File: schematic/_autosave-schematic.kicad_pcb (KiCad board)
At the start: 4 copper layers, 77.8 x 81.6 mm, 154 parts, among them IC1 RS0108YQ20, IC2 AS312, IC3 TPS630250RNCR, IC4 SIM7600G-H_R2, J1 SIM7155-6-1-14-A, J3 USB_C_Receptacle_USB2.0, J9 BATT_CONNECTOR, Q1 BC817, Q10 MMBT3904, Q11 MMBT3904, Q15 SI2302, Q16 SI2302, Q8 NCE6005AR, Q9 NCE6005AR, U10 TPS56339DDC, U2 MT3608, U3 AM2302, U4 TP4056, U6 ESP32-WROOM-32, U8 CH340T(SSOP20W), Y1 12MHz

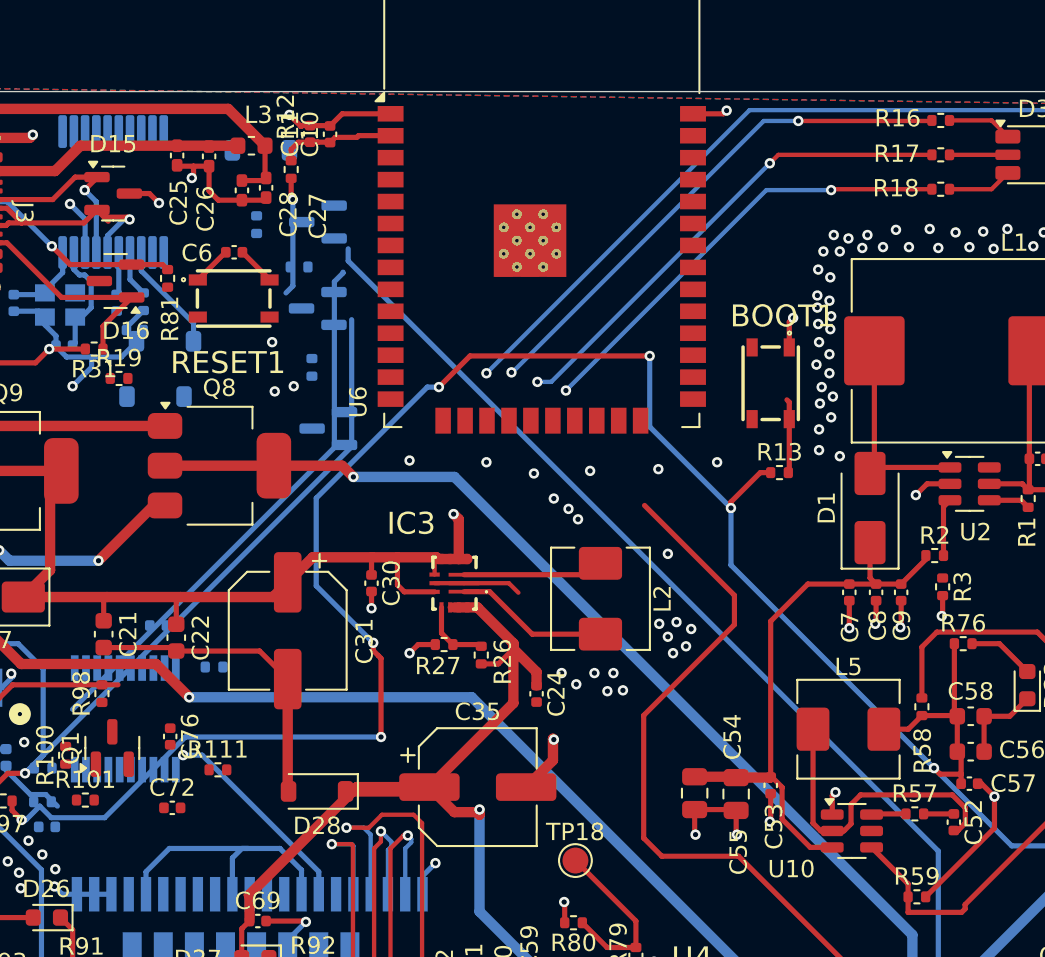
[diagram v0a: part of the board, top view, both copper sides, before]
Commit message: MORE Routing with Global names
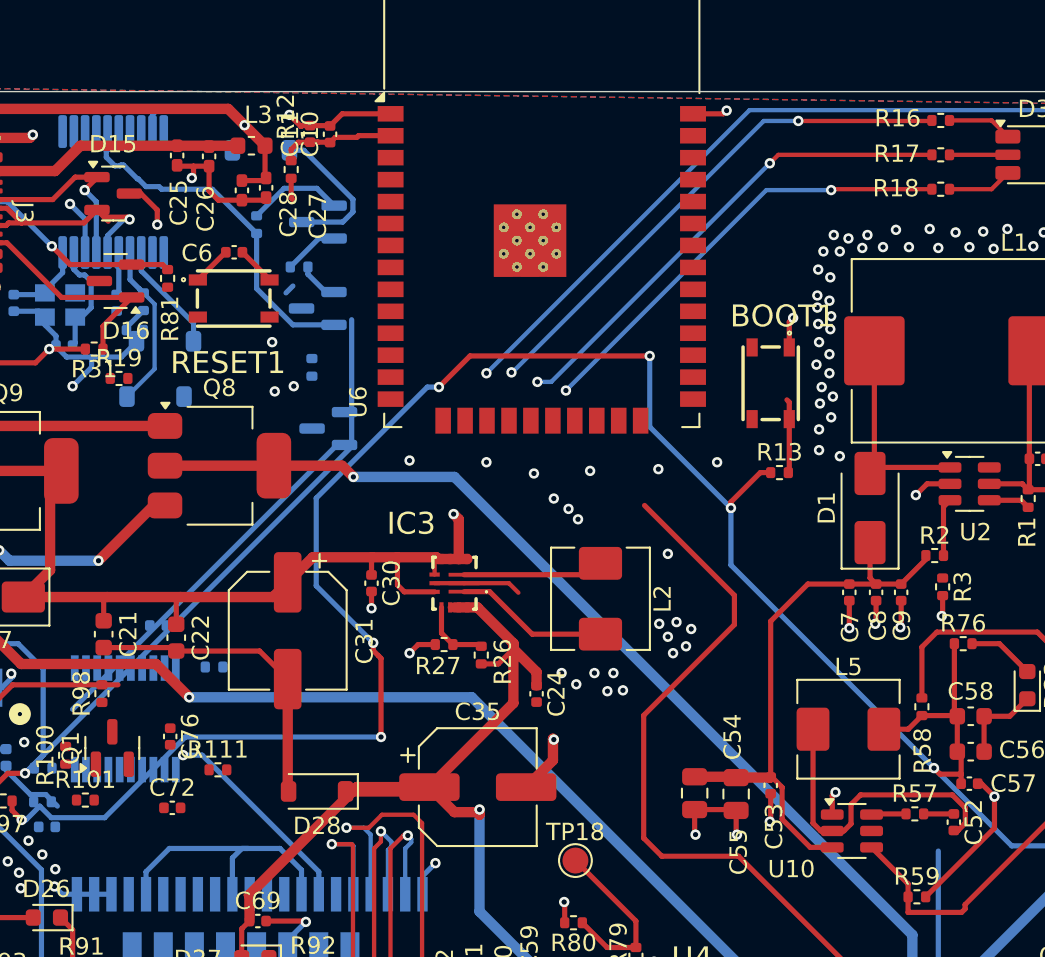
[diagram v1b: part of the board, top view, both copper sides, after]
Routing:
- net /Motion_out: track 63.8 -> 14.8 mm
- net Net-(Q11-E): track 0.00 -> 20.2 mm
- net ESP_TX: track 31.8 -> 21.4 mm
- net Net-(D12-K): track 0.00 -> 8.78 mm
- net Net-(D11-A): track 2.66 -> 9.91 mm
- net +5V: track 206.8 -> 213.6 mm, vias 6 -> 7
- net Net-(Q10-B): track 0.00 -> 5.56 mm
- net /~{esp_rst}: track 9.29 -> 4.29 mm, vias 1 -> 0
- net /dtr: track 0.00 -> 3.22 mm
- net Net-(Q11-B): track 0.00 -> 1.88 mm
- net GND: track 383.2 -> 384.1 mm
